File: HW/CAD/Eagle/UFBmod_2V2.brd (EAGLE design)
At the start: 98.4 x 89.5 mm, 214 parts, among them J1411 ABRACON_ARJE-0034, T0551 MMBT2222, U0501 MIDAS_MCCOG21605B6W-FPTLWI, U0601 MAX5217, U0651 LM4120IM5-3.0, U0701 AT86RF215-ZU, U0711 ASVTX-13-D-26.000MHZ-I05-T, U0811 PE4259, U0821 RFX1010, U0881 B39871B3440U410, U0911 FT232HL, U1101 TPS53353, U1211 TPS62745DSSR, X0891 ANTENNATINY, X0895 ANTENNATINY, X1011 TTE_EN11-HSM, X1311 MOLEX 105017-0001, X1351 PHOENIX_1990067_1X8X2MM50_PTS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, X1361 PHOENIX_1990067_1X8X2MM50_PTS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

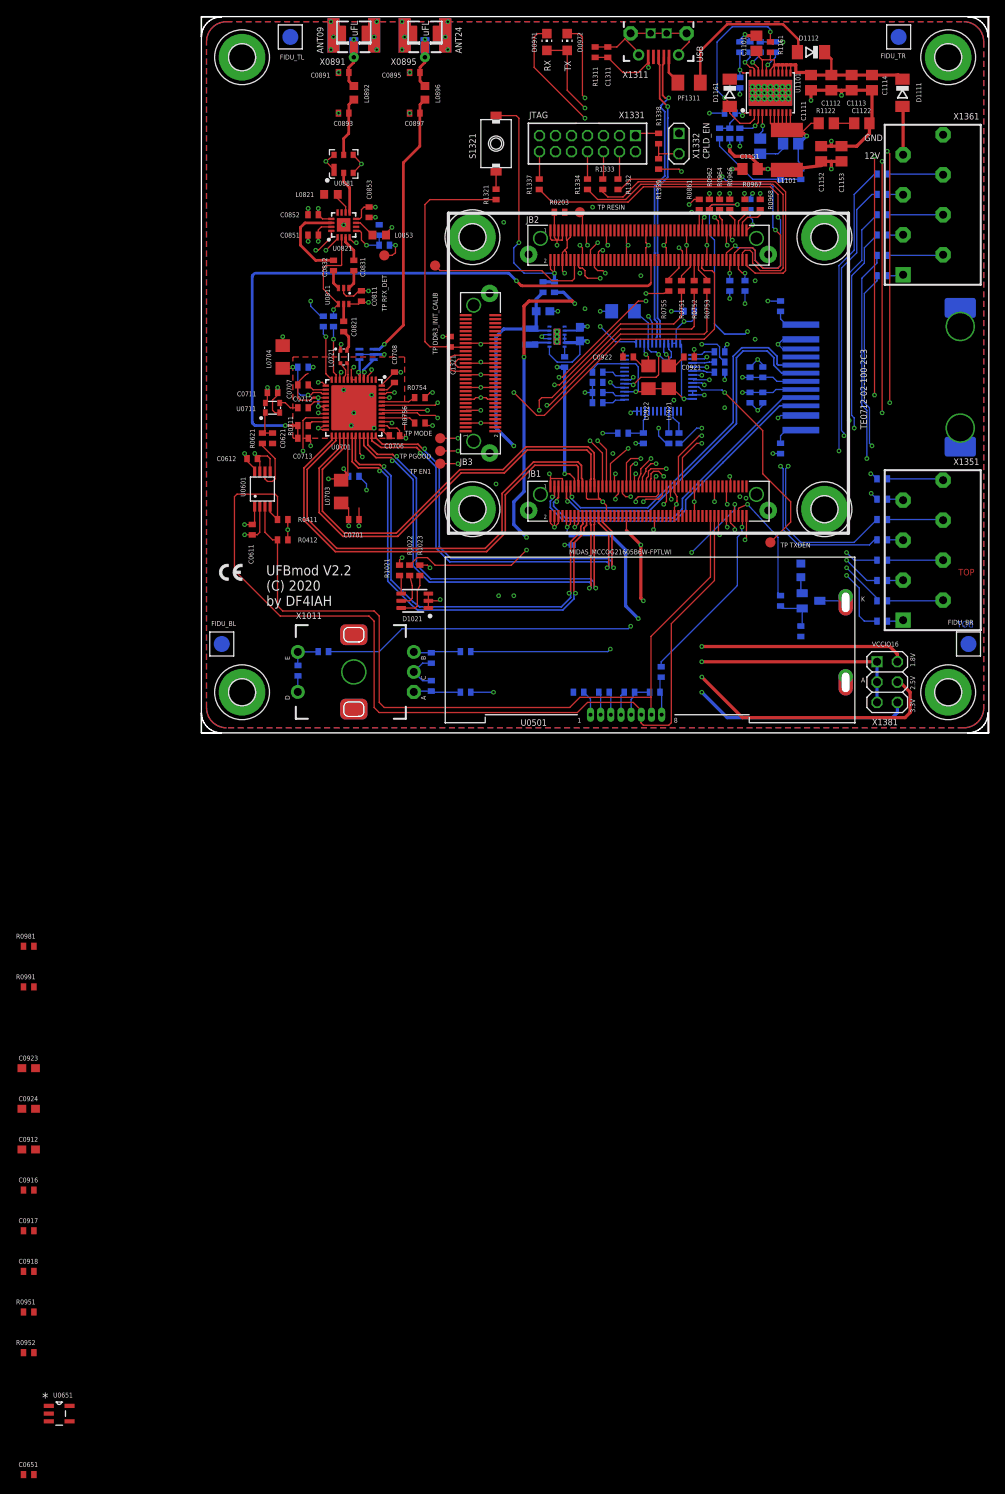
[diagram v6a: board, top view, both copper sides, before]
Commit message: HW - EAGLE - V2.2 devices placed
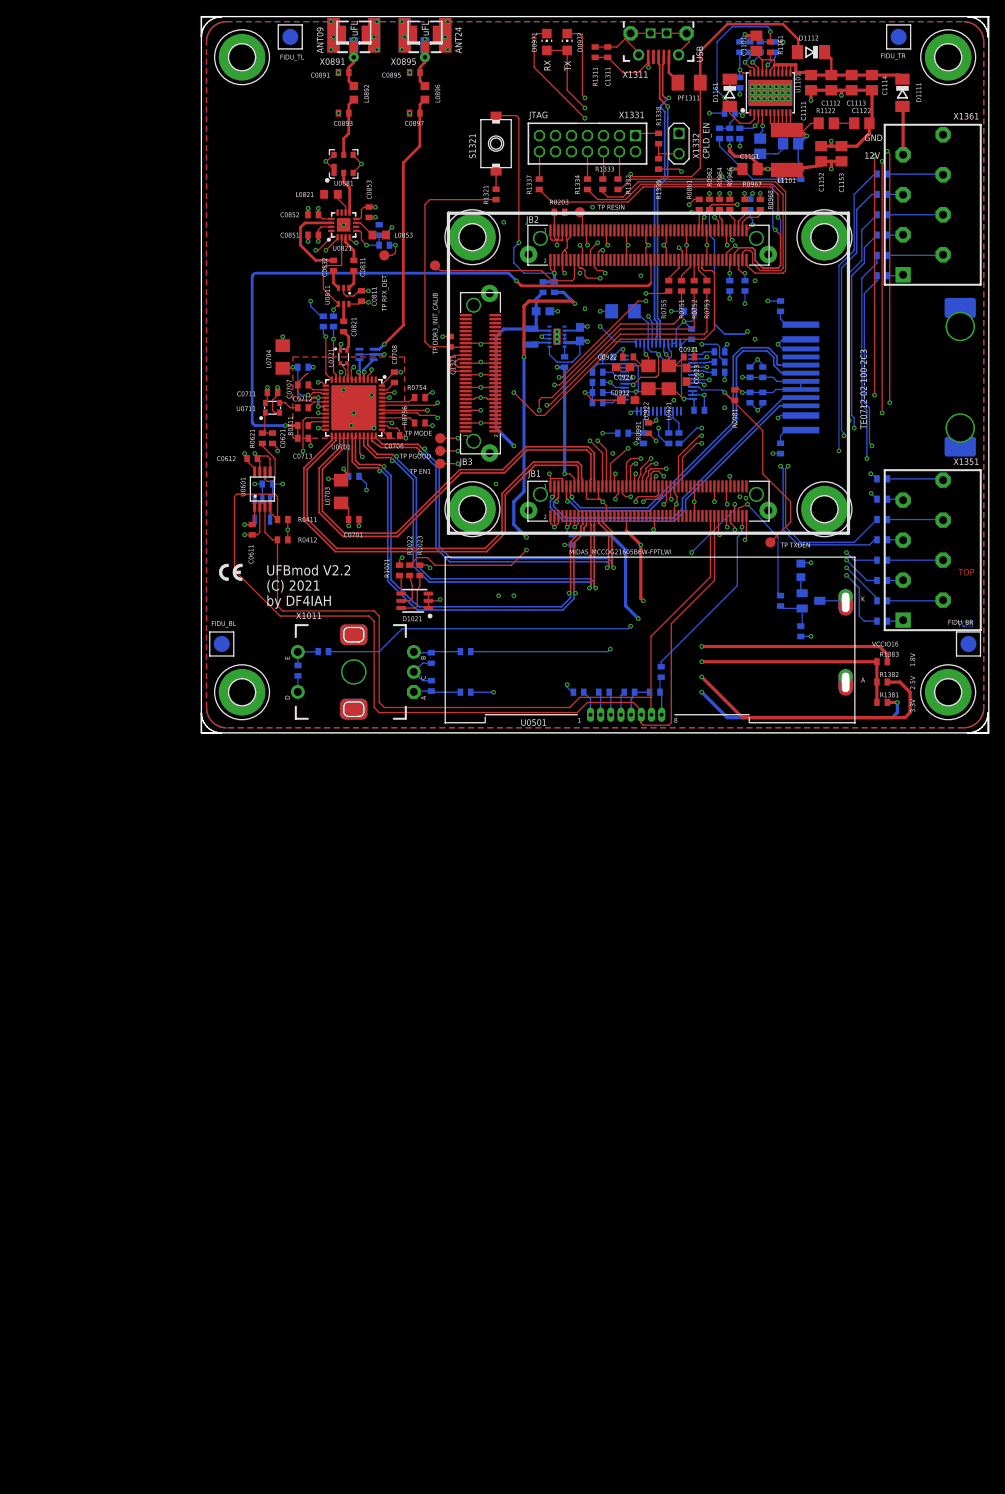
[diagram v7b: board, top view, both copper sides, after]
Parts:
- removed R0951, R0952: 0R, df4iah_rcl:R0402
- removed X1381: (no value), df4iah_connector:2X03
- added R1381: 0R, df4iah_rcl:R0402
- added R1382, R1383: NC, df4iah_rcl:R0402
- moved C0916 135.3 mm to (61.3, 49.8), flipped to the bottom, turned to 90 degrees
- moved C0918 135.3 mm to (50.8, 47.0), flipped to the bottom, turned to 180 degrees
- moved C0917 132.4 mm to (62.2, 40.3), flipped to the bottom, turned to 180 degrees
- moved C0651 127.4 mm to (8.26, 31.1), flipped to the bottom
- moved C0912 119.9 mm to (53.3, 41.6), turned to 180 degrees
- moved C0923 119.5 mm to (60.6, 44.8), turned to 270 degrees
- moved C0924 118.8 mm to (52.7, 45.7), turned to 180 degrees
- moved U0651 115.8 mm to (7.62, 27.9), flipped to the bottom, turned to 270 degrees
- moved R0981 112.0 mm to (66.7, 42.2), turned to 90 degrees
- moved R0991 104.3 mm to (55.9, 38.1), turned to 90 degrees
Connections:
- removed net N$1: R0951.2, U0911.6
- removed net N$3: R0952.2, U0911.7
- net +2V5: now also R1382.2; no longer X1381.4
- net U1V8: now also R1383.2; no longer X1381.2
- net U3V3: now also R1381.2; no longer X1381.6
- net USB_D_N: now also U0911.6; no longer R0951.1
- net USB_D_P: now also U0911.7; no longer R0952.1
- net VCCIO16: now also R1381.1, R1382.1, R1383.1; no longer X1381.1, X1381.3, X1381.5
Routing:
- net +5V_USB: track 20.0 -> 76.2 mm, vias 0 -> 2
- net GND: track 307.5 -> 323.7 mm, vias 101 -> 106
- net +3V3: track 250.8 -> 265.0 mm, vias 26 -> 27
- net FT_VPHY: track 5.38 -> 7.77 mm
- net FT_VPLL: track 5.48 -> 7.80 mm
- net FT_ACBUS7: track 0.00 -> 2.28 mm, vias 0 -> 1
- net FT_TXDEN: track 27.5 -> 29.1 mm
- net +3V0_20MHZ_VCTCXO: track 3.36 -> 4.87 mm
- net U1V8: track 101.6 -> 100.3 mm
- net +2V5: track 107.0 -> 108.3 mm
- net U3V3: track 118.7 -> 120.0 mm, vias 6 -> 7
- net USB_D_P: track 36.1 -> 36.9 mm
- net USB_D_N: track 37.0 -> 37.7 mm
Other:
- board text added: "UFBmod V2.2 (C) 2021 by DF4IAH"
- board text removed: "UFBmod V2.2 (C) 2020 by DF4IAH"
